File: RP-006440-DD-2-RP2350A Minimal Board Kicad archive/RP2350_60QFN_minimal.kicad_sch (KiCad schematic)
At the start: 44 parts, among them J1 USB_C_Receptacle_USB2.0_16P, J2 Conn_02x18_Odd_Even, J3 Conn_02x18_Odd_Even, SW1 SW_Push, SW2 SW_Push, U1 RP2350_60QFN, U2 NCP1117-3.3_SOT223, U3 W25Q128JVS, Y1 ABM8-272-T3

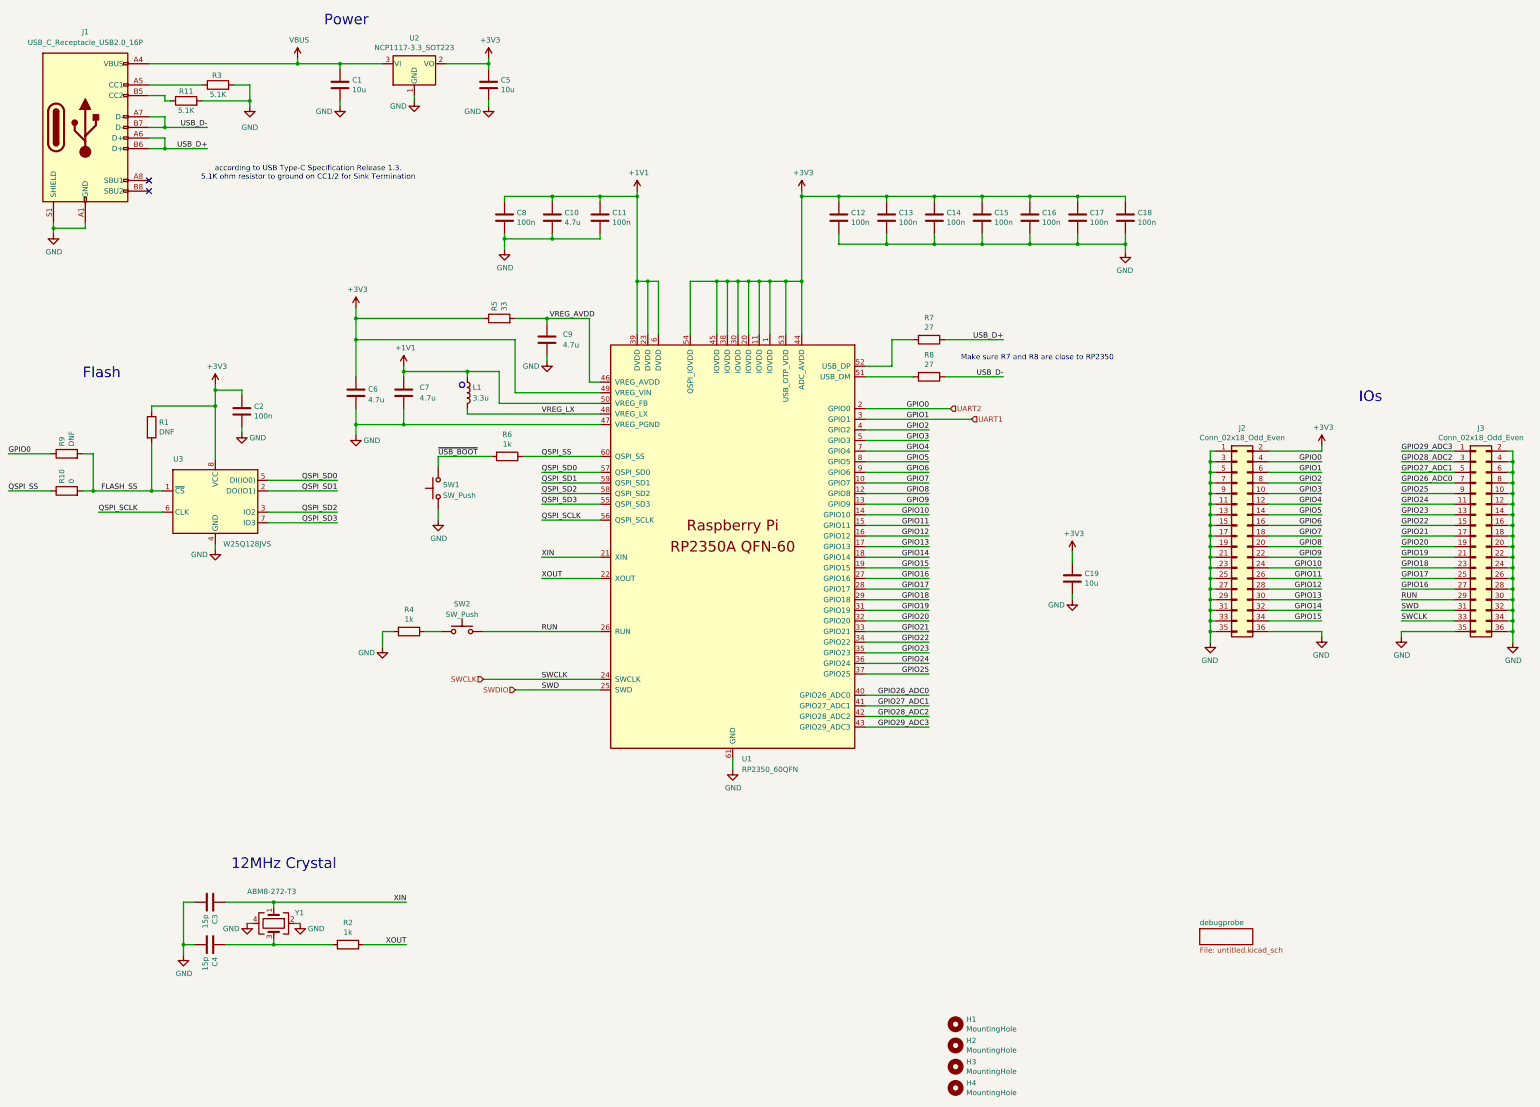
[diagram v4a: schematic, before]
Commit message: Update schematic and PCB
Added hierarchal labels between main and debugprobe, connected the pins.
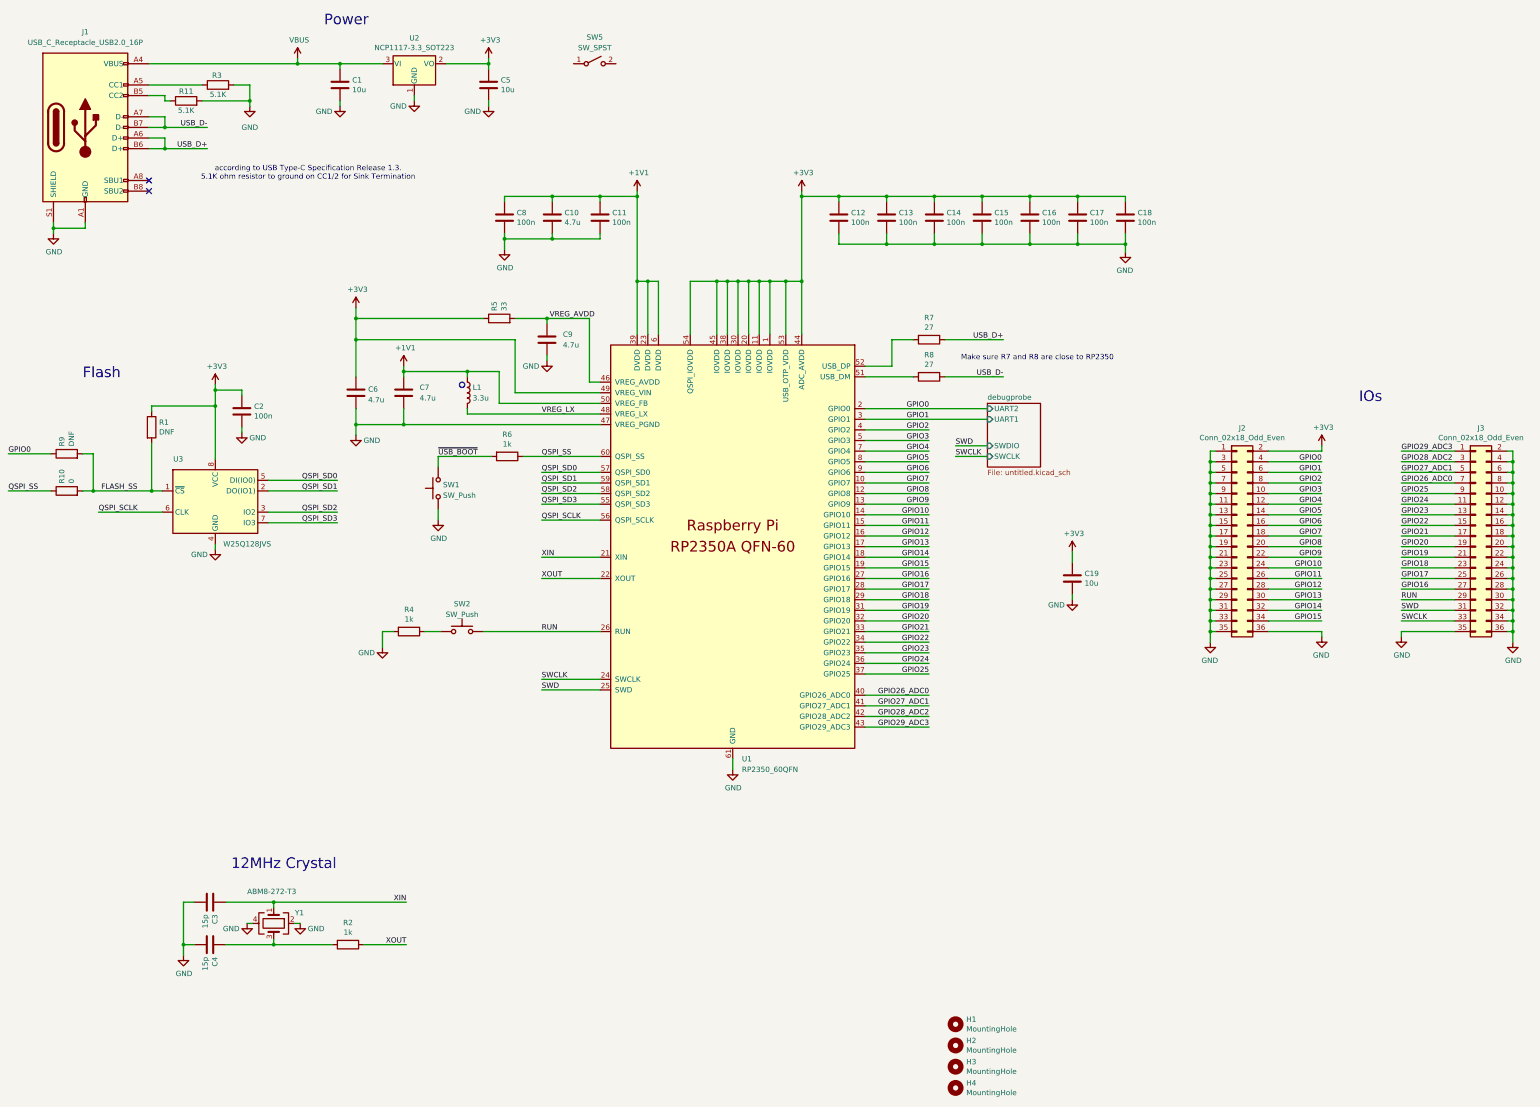
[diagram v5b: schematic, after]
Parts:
- added SW5: SW_SPST, Button_Switch_SMD:SW_DPDT_CK_JS202011JCQN, symbol Switch:SW_SPST
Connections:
- net SWDIO renamed SWD
- net UART1 renamed GPIO1
- net UART2 renamed GPIO0
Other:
- sheet debugprobe ports: added SWCLK, SWDIO, UART1, UART2; removed none
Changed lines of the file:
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@@
 	(wire
 		(pts
-			(xy 229.87 111.76) (xy 250.19 111.76)
+			(xy 229.87 111.76) (xy 259.08 111.76)
 		)
 		(stroke
@@
 	(wire
 		(pts
-			(xy 166.37 176.53) (xy 138.43 176.53)
+			(xy 166.37 176.53) (xy 152.4 176.53)
 		)
 		(stroke
@@
 	(wire
 		(pts
-			(xy 229.87 114.3) (xy 255.27 114.3)
+			(xy 229.87 114.3) (xy 259.08 114.3)
 		)
 		(stroke
@@
 	(wire
 		(pts
-			(xy 146.05 179.07) (xy 166.37 179.07)
-		)
-		(stroke
-			(width 0)
-			(type default)
-		)
-	)
-	(wire
-		(pts
 			(xy 269.24 62.23) (xy 269.24 60.96)
 		)
@@
 	(wire
 		(pts
+			(xy 251.46 123.19) (xy 259.08 123.19)
+		)
+		(stroke
+			(width 0)
+			(type default)
+		)
+	)
+	(wire
+		(pts
 			(xy 134.62 113.03) (xy 134.62 111.76)
 		)
@@
 	(wire
 		(pts
+			(xy 152.4 179.07) (xy 166.37 179.07)
+		)
+		(stroke
+			(width 0)
+			(type default)
+		)
+	)
+	(wire
+		(pts
 			(xy 384.81 147.32) (xy 384.81 149.86)
 		)
@@
 		)
 	)
+	(wire
+		(pts
+			(xy 251.46 120.65) (xy 259.08 120.65)
+		)
+		(stroke
+			(width 0)
+			(type default)
+		)
+	)
 	(circle
 		(center 133.35 106.045)
@@
 		)
 	)
+	(label "SWCLK"
+		(at 152.4 176.53 0)
+		(effects
+			(font
+				(size 1.27 1.27)
+			)
+			(justify left bottom)
+		)
+	)
 	(label "GPIO1"
 		(at 245.11 114.3 180)
@@
 		)
 	)
-	(label "SWCLK"
-		(at 152.4 176.53 0)
+	(label "SWD"
+		(at 251.46 120.65 0)
 		(effects
 			(font
@@
 		)
 	)
+	(label "SWCLK"
+		(at 251.46 123.19 0)
+		(effects
+			(font
+				(size 1.27 1.27)
+			)
+			(justify left bottom)
+		)
+	)
 	(label "GPIO10"
 		(at 245.11 137.16 180)
@@
 		)
 	)
-	(hierarchical_label "SWDIO"
-		(shape input)
-		(at 146.05 179.07 180)
-		(effects
-			(font
-				(size 1.27 1.27)
-			)
-			(justify right)
-		)
-	)
-	(hierarchical_label "UART1"
-		(shape input)
-		(at 255.27 114.3 0)
-		(effects
-			(font
-				(size 1.27 1.27)
-			)
-			(justify left)
-		)
-	)
-	(hierarchical_label "SWCLK"
-		(shape input)
-		(at 138.43 176.53 180)
-		(effects
-			(font
-				(size 1.27 1.27)
-			)
-			(justify right)
-		)
-	)
-	(hierarchical_label "UART2"
-		(shape input)
-		(at 250.19 111.76 0)
-		(effects
-			(font
-				(size 1.27 1.27)
-			)
-			(justify left)
-		)
-	)
 	(symbol
 		(lib_id "Memory_Flash:W25Q128JVS")
@@
 	)
 	(symbol
+		(lib_id "Switch:SW_SPST")
+		(at 165.1 29.21 0)
+		(unit 1)
+		(exclude_from_sim no)
+		(in_bom yes)
+		(on_board yes)
+		(dnp no)
+		(fields_autoplaced yes)
+		(property "Reference" "SW5"
+			(at 165.1 22.86 0)
+			(effects
+				(font
+					(size 1.27 1.27)
+				)
+			)
+		)
+		(property "Value" "SW_SPST"
+			(at 165.1 25.4 0)
+			(effects
+				(font
+					(size 1.27 1.27)
+				)
+			)
+		)
+		(property "Footprint" "Button_Switch_SMD:SW_DPDT_CK_JS202011JCQN"
+			(at 165.1 29.21 0)
+			(effects
+				(font
+					(size 1.27 1.27)
+				)
+				(hide yes)
+			)
+		)
+		(property "Datasheet" "~"
+			(at 165.1 29.21 0)
+			(effects
+				(font
+					(size 1.27 1.27)
+				)
+				(hide yes)
+			)
+		)
+		(property "Description" "Single Pole Single Throw (SPST) switch"
+			(at 165.1 29.21 0)
+			(effects
+				(font
+					(size 1.27 1.27)
+				)
+				(hide yes)
+			)
+		)
+		(pin "1"
+		)
+		(pin "2"
+		)
+		(instances
+			(project ""
+				(path "/94683f5c-9cd9-448e-be96-9792537b5cb8"
+					(reference "SW5")
+					(unit 1)
+				)
+			)
+		)
+	)
+	(symbol
 		(lib_name "GND_1")
 		(lib_id "power:GND")
@@
 	)
 	(sheet
-		(at 309.88 236.22)
-		(size 12.7 3.81)
+		(at 259.08 110.49)
+		(size 12.7 15.24)
 		(fields_autoplaced yes)
 		(stroke
@@
 		)
 		(property "Sheetname" "debugprobe"
-			(at 309.88 235.5084 0)
+			(at 259.08 109.7784 0)
 			(effects
 				(font
@@
 		)
 		(property "Sheetfile" "untitled.kicad_sch"
-			(at 309.88 240.6146 0)
+			(at 259.08 126.3146 0)
 			(effects
 				(font
@@
 			)
 		)
+		(pin "SWCLK" input
+			(at 259.08 123.19 180)
+			(effects
+				(font
+					(size 1.27 1.27)
+				)
+				(justify left)
+			)
+		)
+		(pin "SWDIO" input
+			(at 259.08 120.65 180)
+			(effects
+				(font
+					(size 1.27 1.27)
+				)
+				(justify left)
+			)
+		)
+		(pin "UART1" input
+			(at 259.08 114.3 180)
+			(effects
+				(font
+					(size 1.27 1.27)
+				)
+				(justify left)
+			)
+		)
+		(pin "UART2" input
+			(at 259.08 111.76 180)
+			(effects
+				(font
+					(size 1.27 1.27)
+				)
+				(justify left)
+			)
+		)

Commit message: Small change
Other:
- moved on the sheet: C19
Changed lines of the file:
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@@
 	(wire
 		(pts
-			(xy 229.87 111.76) (xy 259.08 111.76)
+			(xy 143.51 69.85) (xy 143.51 71.12)
 		)
 		(stroke
@@
 	(wire
 		(pts
-			(xy 143.51 69.85) (xy 143.51 71.12)
+			(xy 93.98 27.94) (xy 93.98 29.21)
 		)
 		(stroke
@@
 	(wire
 		(pts
-			(xy 93.98 27.94) (xy 93.98 29.21)
+			(xy 153.67 90.17) (xy 163.83 90.17)
 		)
 		(stroke
@@
 	(wire
 		(pts
-			(xy 153.67 90.17) (xy 163.83 90.17)
+			(xy 384.81 154.94) (xy 384.81 157.48)
 		)
 		(stroke
@@
 	(wire
 		(pts
-			(xy 384.81 154.94) (xy 384.81 157.48)
+			(xy 229.87 114.3) (xy 245.11 114.3)
 		)
 		(stroke
@@
 	(wire
 		(pts
+			(xy 273.05 201.93) (xy 280.67 201.93)
+		)
+		(stroke
+			(width 0)
+			(type default)
+		)
+	)
+	(wire
+		(pts
 			(xy 104.14 30.48) (xy 104.14 29.21)
 		)
@@
 	(wire
 		(pts
-			(xy 229.87 114.3) (xy 259.08 114.3)
-		)
-		(stroke
-			(width 0)
-			(type default)
-		)
-	)
-	(wire
-		(pts
 			(xy 86.995 139.065) (xy 103.505 139.065)
 		)
@@
 	(wire
 		(pts
-			(xy 279.4 146.05) (xy 279.4 148.59)
+			(xy 314.96 64.77) (xy 314.96 67.31)
 		)
 		(stroke
@@
 	(wire
 		(pts
+			(xy 229.87 111.76) (xy 245.11 111.76)
+		)
+		(stroke
+			(width 0)
+			(type default)
+		)
+	)
+	(wire
+		(pts
 			(xy 312.42 129.54) (xy 312.42 132.08)
 		)
@@
 	(wire
 		(pts
-			(xy 251.46 123.19) (xy 259.08 123.19)
+			(xy 273.05 210.82) (xy 280.67 210.82)
 		)
 		(stroke
@@
 	(wire
 		(pts
+			(xy 273.05 199.39) (xy 280.67 199.39)
+		)
+		(stroke
+			(width 0)
+			(type default)
+		)
+	)
+	(wire
+		(pts
 			(xy 194.31 81.28) (xy 196.85 81.28)
 		)
@@
 	(wire
 		(pts
-			(xy 279.4 156.21) (xy 279.4 157.48)
+			(xy 314.96 74.93) (xy 314.96 76.2)
 		)
 		(stroke
@@
 	(wire
 		(pts
-			(xy 251.46 120.65) (xy 259.08 120.65)
+			(xy 273.05 208.28) (xy 280.67 208.28)
 		)
 		(stroke
@@
 		)
 	)
+	(label "GPIO1"
+		(at 273.05 201.93 0)
+		(effects
+			(font
+				(size 1.27 1.27)
+			)
+			(justify left bottom)
+		)
+	)
 	(label "GPIO0"
 		(at 245.11 111.76 180)
@@
 	)
 	(label "SWD"
-		(at 251.46 120.65 0)
+		(at 273.05 208.28 0)
 		(effects
 			(font
@@
 	)
 	(label "SWCLK"
-		(at 251.46 123.19 0)
+		(at 273.05 210.82 0)
 		(effects
 			(font
@@
 		)
 	)
+	(label "GPIO0"
+		(at 273.05 199.39 0)
+		(effects
+			(font
+				(size 1.27 1.27)
+			)
+			(justify left bottom)
+		)
+	)
 	(label "GPIO13"
 		(at 339.09 157.48 180)
@@
 	(symbol
 		(lib_id "power:+3V3")
-		(at 279.4 146.05 0)
+		(at 314.96 64.77 0)
 		(unit 1)
 		(exclude_from_sim no)
@@
 		(dnp no)
 		(property "Reference" "#PWR027"
-			(at 279.4 149.86 0)
+			(at 314.96 68.58 0)
 			(effects
 				(font
@@
 		)
 		(property "Value" "+3V3"
-			(at 279.781 141.6558 0)
+			(at 315.341 60.3758 0)
 			(effects
 				(font
@@
 		)
 		(property "Footprint" ""
-			(at 279.4 146.05 0)
+			(at 314.96 64.77 0)
 			(effects
 				(font
@@
 		)
 		(property "Datasheet" ""
-			(at 279.4 146.05 0)
+			(at 314.96 64.77 0)
 			(effects
 				(font
@@
 		)
 		(property "Description" ""
-			(at 279.4 146.05 0)
+			(at 314.96 64.77 0)
 			(effects
 				(font
@@
 	(symbol
 		(lib_id "Device:C")
-		(at 279.4 152.4 0)
+		(at 314.96 71.12 0)
 		(unit 1)
 		(exclude_from_sim no)
@@
 		(dnp no)
 		(property "Reference" "C19"
-			(at 282.321 151.2316 0)
+			(at 317.881 69.9516 0)
 			(effects
 				(font
@@
 		)
 		(property "Value" "10u"
-			(at 282.321 153.543 0)
+			(at 317.881 72.263 0)
 			(effects
 				(font
@@
 		)
 		(property "Footprint" "Capacitor_SMD:C_0805_2012Metric"
-			(at 280.3652 156.21 0)
+			(at 315.9252 74.93 0)
 			(effects
 				(font
@@
 		)
 		(property "Datasheet" "~"
-			(at 279.4 152.4 0)
+			(at 314.96 71.12 0)
 			(effects
 				(font
@@
 		)
 		(property "Description" ""
-			(at 279.4 152.4 0)
+			(at 314.96 71.12 0)
 			(effects
 				(font
@@
 	(symbol
 		(lib_id "power:GND")
-		(at 279.4 157.48 0)
+		(at 314.96 76.2 0)
 		(unit 1)
 		(exclude_from_sim no)
@@
 		(dnp no)
 		(property "Reference" "#PWR028"
-			(at 279.4 163.83 0)
+			(at 314.96 82.55 0)
 			(effects
 				(font
@@
 		)
 		(property "Value" "GND"
-			(at 275.59 158.75 0)
+			(at 311.15 77.47 0)
 			(effects
 				(font
@@
 		)
 		(property "Footprint" ""
-			(at 279.4 157.48 0)
+			(at 314.96 76.2 0)
 			(effects
 				(font
@@
 		)
 		(property "Datasheet" ""
-			(at 279.4 157.48 0)
+			(at 314.96 76.2 0)
 			(effects
 				(font
@@
 		)
 		(property "Description" ""
-			(at 279.4 157.48 0)
+			(at 314.96 76.2 0)
 			(effects
 				(font
@@
 	)
 	(sheet
-		(at 259.08 110.49)
+		(at 280.67 198.12)
 		(size 12.7 15.24)
 		(fields_autoplaced yes)
@@
 		)
 		(property "Sheetname" "debugprobe"
-			(at 259.08 109.7784 0)
+			(at 280.67 197.4084 0)
 			(effects
 				(font
@@
 		)
 		(property "Sheetfile" "untitled.kicad_sch"
-			(at 259.08 126.3146 0)
+			(at 280.67 213.9446 0)
 			(effects
 				(font
@@
 		)
 		(pin "SWCLK" input
-			(at 259.08 123.19 180)
+			(at 280.67 210.82 180)
 			(effects
 				(font
@@
 		)
 		(pin "SWDIO" input
-			(at 259.08 120.65 180)
+			(at 280.67 208.28 180)
 			(effects
 				(font
@@
 		)
 		(pin "UART1" input
-			(at 259.08 114.3 180)
+			(at 280.67 201.93 180)
 			(effects
 				(font
@@
 		)
 		(pin "UART2" input
-			(at 259.08 111.76 180)
+			(at 280.67 199.39 180)
 			(effects
 				(font
